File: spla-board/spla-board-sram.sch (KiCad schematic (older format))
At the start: 0 parts

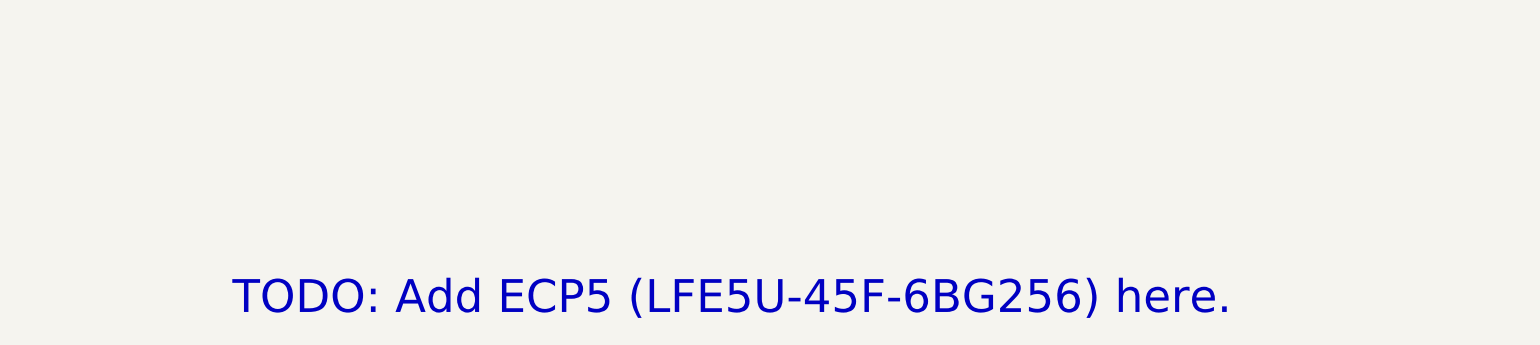
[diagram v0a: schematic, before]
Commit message: schematic: Add blank sheets for future components; rearrange root sheet.
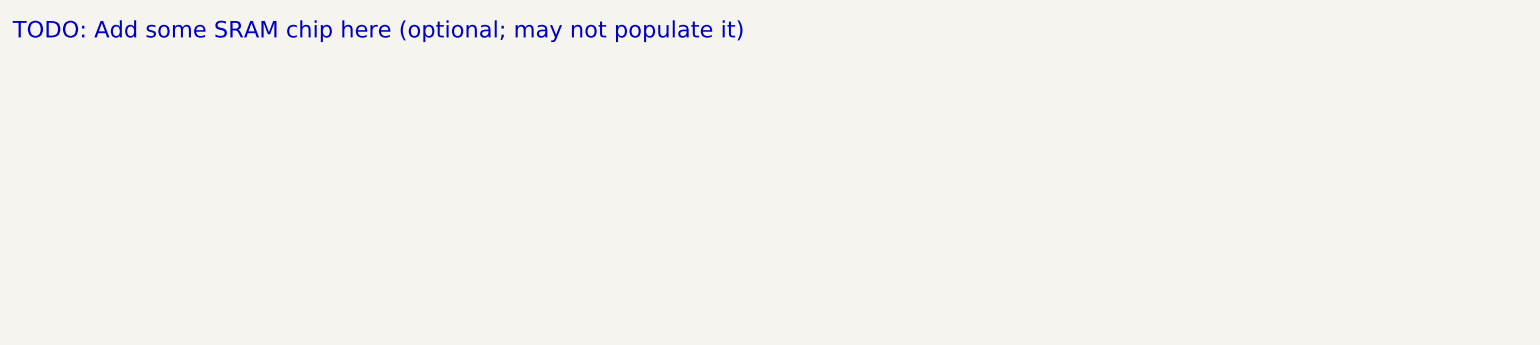
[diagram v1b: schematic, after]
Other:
- note added: "TODO: Add some SRAM chip here (optional; may not populate it)"
- note removed: "TODO: Add ECP5 (LFE5U-45F-6BG256) here."
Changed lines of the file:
@@
 EELAYER 30 0
 EELAYER END
-$Descr A3 16535 11693
+$Descr A4 11693 8268
 encoding utf-8
-Sheet 3 8
-Title "SPLA Board - FPGA"
+Sheet 7 8
+Title ""
 Date "2020-02-21"
 Rev "3"
@@
 Comment4 ""
 $EndDescr
-Text Notes 4900 5650 0    202  ~ 0
-TODO: Add ECP5 (LFE5U-45F-6BG256) here.
+Text Notes 3550 3950 0    101  ~ 0
+TODO: Add some SRAM chip here (optional; may not populate it)
 $EndSCHEMATC

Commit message: schematic: Change all pages to A3; open up layout for level shifters.
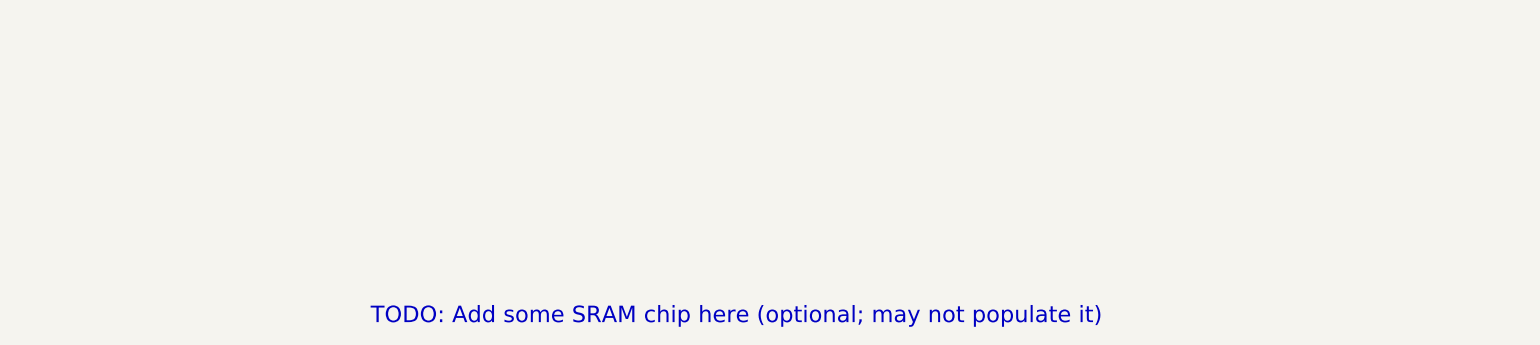
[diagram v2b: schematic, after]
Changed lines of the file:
@@
 EELAYER 30 0
 EELAYER END
-$Descr A4 11693 8268
+$Descr A3 16535 11693
 encoding utf-8
-Sheet 7 8
+Sheet 8 8
 Title ""
 Date "2020-02-21"
@@
 Comment4 ""
 $EndDescr
-Text Notes 3550 3950 0    101  ~ 0
+Text Notes 5750 5700 0    101  ~ 0
 TODO: Add some SRAM chip here (optional; may not populate it)
 $EndSCHEMATC
